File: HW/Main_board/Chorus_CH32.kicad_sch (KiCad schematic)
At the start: 88 parts, among them J1 DC_Jack, J2 Prog_Head, J3 Footswitch, J4 IN, J5 OUT, J6 Pot1, J7 Pot2, J8 UART, J9 9V, K1 G6KU-2, U1 AMS1117-5.0, U4 74LVC2G00, U6 TL072, U7 TL072, U8 TL072, U9 CH32V003AxMx

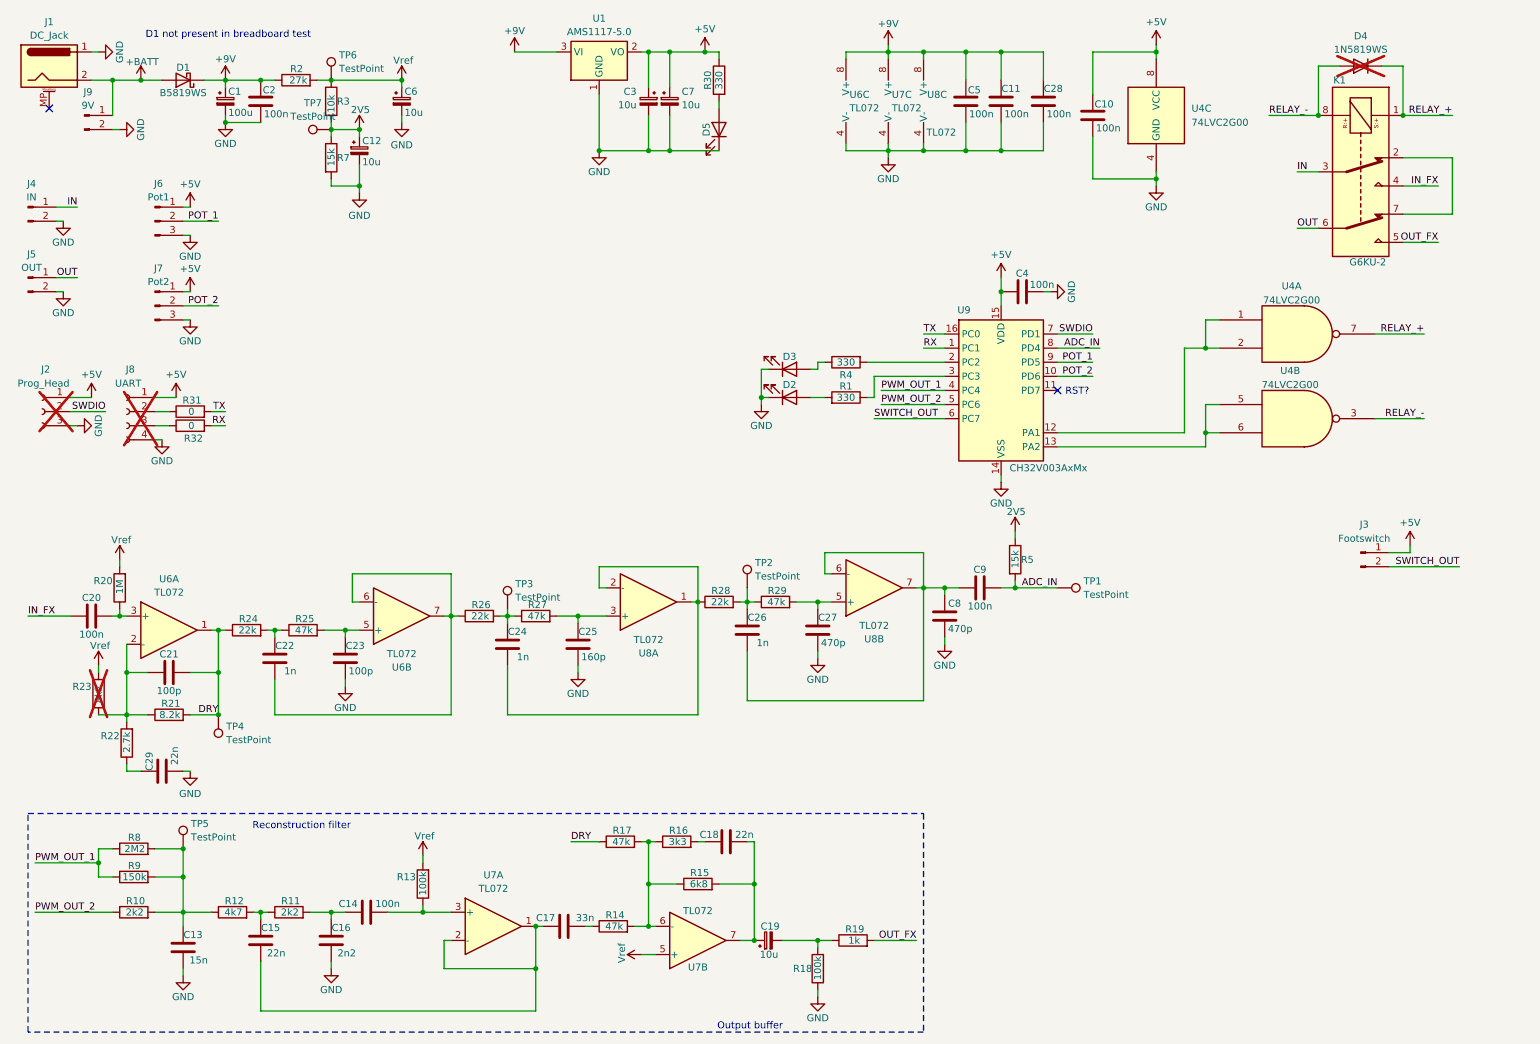
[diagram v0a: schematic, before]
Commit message: working passthrough code with dma + ouput buffer HW
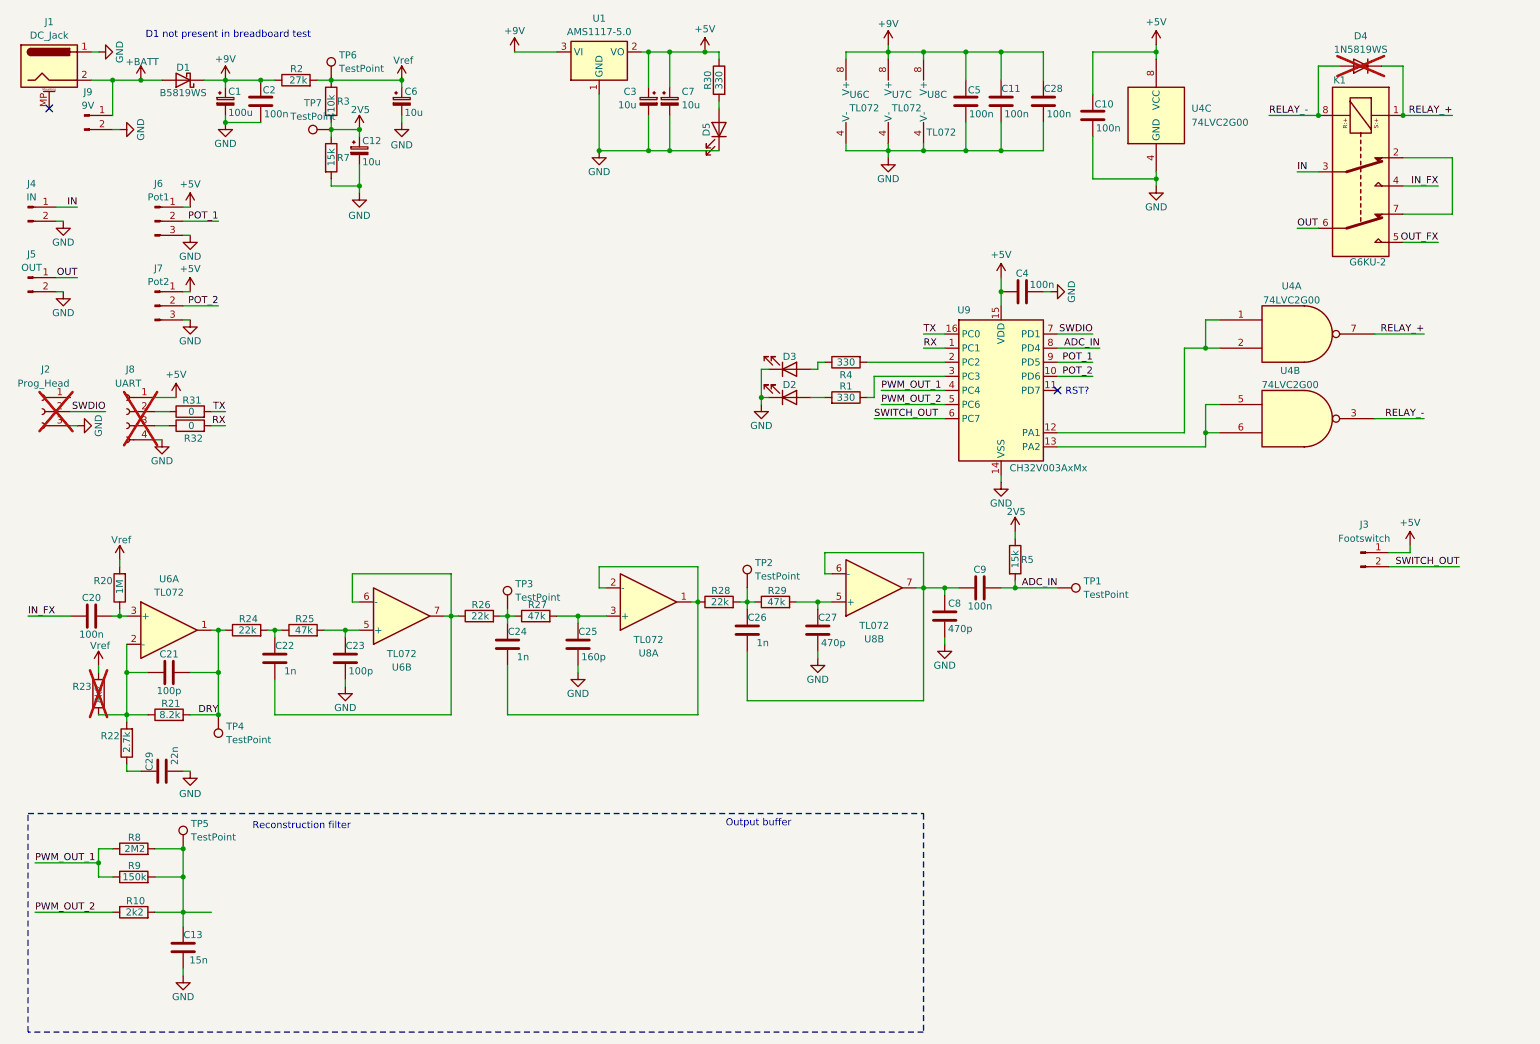
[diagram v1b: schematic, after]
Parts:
- removed C14: 100n, Capacitor_SMD:C_0603_1608Metric, symbol Device:C
- removed C15, C18: 22n, Capacitor_SMD:C_0603_1608Metric, symbol Device:C
- removed C16: 2n2, Capacitor_SMD:C_0603_1608Metric, symbol Device:C
- removed C17: 33n, Capacitor_SMD:C_0603_1608Metric, symbol Device:C
- removed C19: 10u, Capacitor_SMD:CP_Elec_5x5.4, symbol Device:C_Polarized_Small
- removed R11: 2k2, Resistor_SMD:R_0603_1608Metric, symbol Device:R
- removed R12: 4k7, Resistor_SMD:R_0603_1608Metric, symbol Device:R
- removed R13, R18: 100k, Resistor_SMD:R_0603_1608Metric, symbol Device:R
- removed R14, R17: 47k, Resistor_SMD:R_0603_1608Metric, symbol Device:R
- removed R15: 6k8, Resistor_SMD:R_0603_1608Metric, symbol Device:R
- removed R16: 3k3, Resistor_SMD:R_0603_1608Metric, symbol Device:R
- removed R19: 1k, Resistor_SMD:R_0603_1608Metric, symbol Device:R
- removed unit 1 of U7
- removed unit 2 of U7
- J3, J4, J5: footprint Connector_JST:JST_PH_B2B-PH-K_1x02_P2.00mm_Vertical -> Connector_PinHeader_2.54mm:PinHeader_1x02_P2.54mm_Vertical
- J6, J7: footprint Connector_JST:JST_PH_B3B-PH-K_1x03_P2.00mm_Vertical -> Connector_PinHeader_2.54mm:PinHeader_1x02_P2.54mm_Vertical
- J9: footprint Connector_JST:JST_PH_B2B-PH-K_1x02_P2.00mm_Vertical -> Connector_PinSocket_2.54mm:PinSocket_1x02_P2.54mm_Vertical
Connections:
- net +5V: no longer J2.1 (Pin_1)

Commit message: correction on output board and new main layout/schem
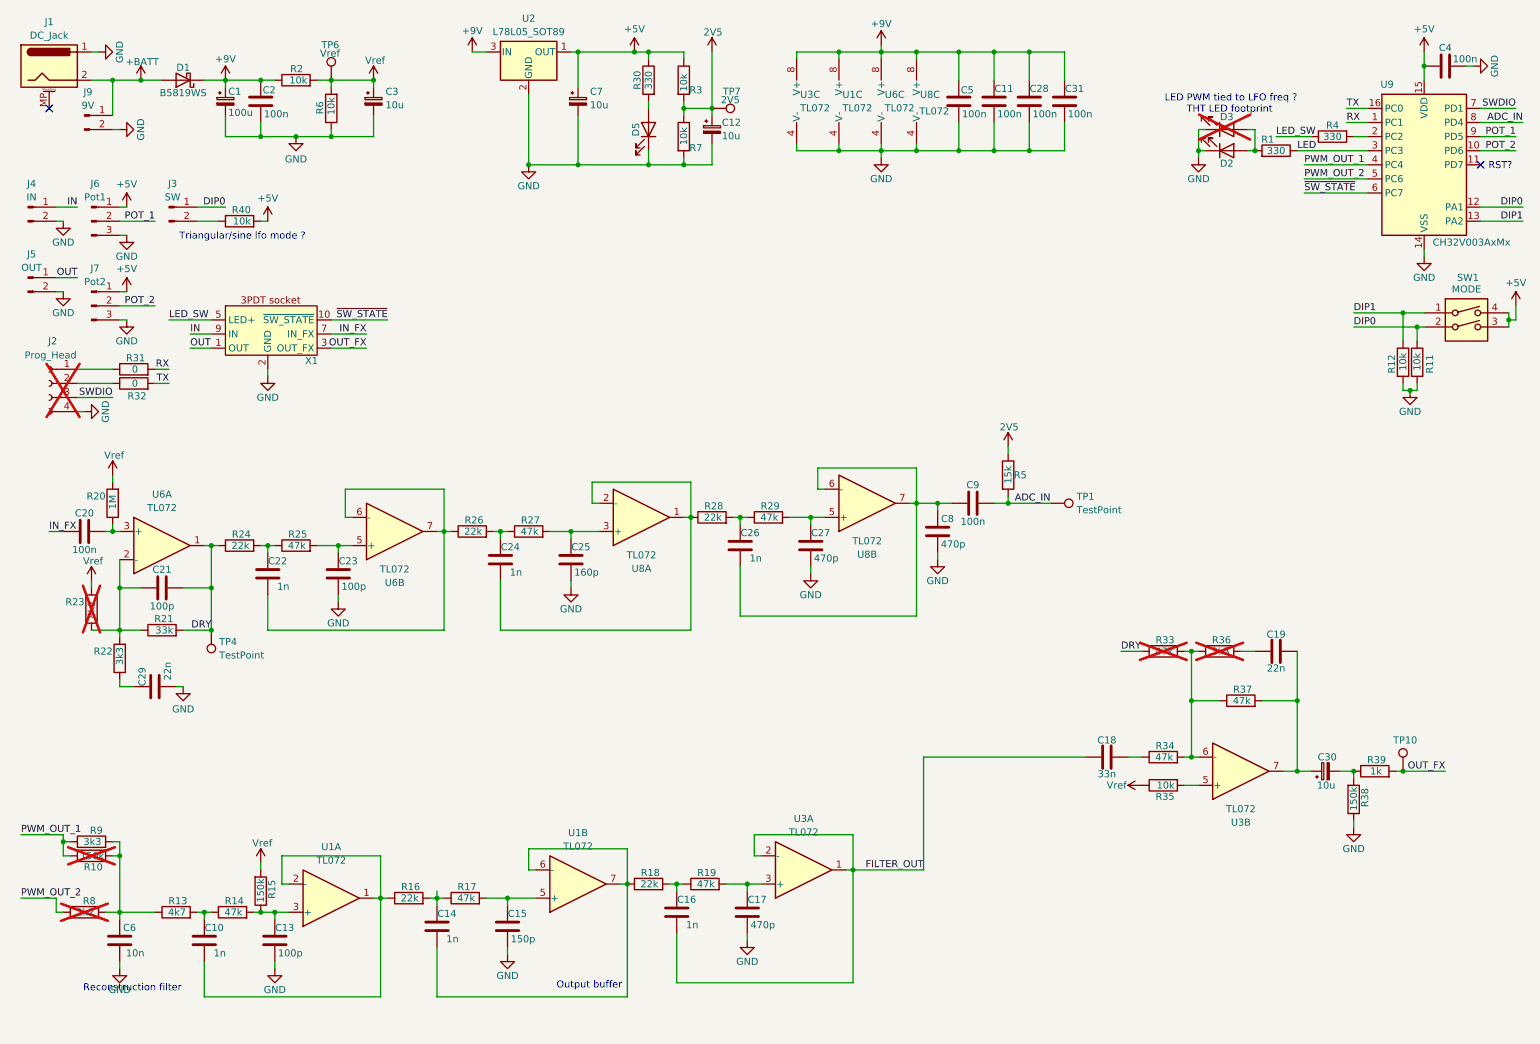
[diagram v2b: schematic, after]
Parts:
- removed C6: 10u, Capacitor_SMD:CP_Elec_5x5.4, symbol Device:C_Polarized_Small
- removed D4: 1N5819WS, Diode_SMD:D_SOD-323, symbol Device:D
- removed J8: UART, Connector_PinHeader_2.54mm:PinHeader_1x04_P2.54mm_Vertical, symbol Connector:Conn_01x04_Socket
- removed K1: G6KU-2, Relay_SMD:Relay_DPDT_Omron_G6K-2F-Y, symbol Relay:G6KU-2
- removed TP2, TP3, TP5: TestPoint, TestPoint:TestPoint_Pad_D1.0mm, symbol Connector:TestPoint
- removed U1: AMS1117-5.0, Package_TO_SOT_SMD:SOT-223-3_TabPin2, symbol Regulator_Linear:AMS1117-5.0
- removed U4: 74LVC2G00, Package_SO:VSSOP-8_2.3x2mm_P0.5mm, symbol 74xGxx:74LVC2G00
- removed U7: TL072, Package_SO:SOIC-8_3.9x4.9mm_P1.27mm, symbol Amplifier_Operational:TL072
- added C14, C16: 1n, Capacitor_SMD:C_0603_1608Metric, symbol Device:C
- added C15: 150p, Capacitor_SMD:C_0603_1608Metric, symbol Device:C
- added C17: 470p, Capacitor_SMD:C_0603_1608Metric, symbol Device:C
- added C18: 33n, Capacitor_SMD:C_0603_1608Metric, symbol Device:C
- added C19: 22n, Capacitor_SMD:C_0603_1608Metric, symbol Device:C
- added C30: 10u, Capacitor_SMD:CP_Elec_5x5.4, symbol Device:C_Polarized_Small
- added C31: 100n, Capacitor_SMD:C_0603_1608Metric, symbol Device:C
- added C6: 10n, Capacitor_SMD:C_0603_1608Metric, symbol Device:C
- added R11, R12, R35, R40, R6: 10k, Resistor_SMD:R_0603_1608Metric, symbol Device:R
- added R13: 4k7, Resistor_SMD:R_0603_1608Metric, symbol Device:R
- added R14, R17, R19, R33, R34, R37: 47k, Resistor_SMD:R_0603_1608Metric, symbol Device:R
- added R15, R38: 150k, Resistor_SMD:R_0603_1608Metric, symbol Device:R
- added R16, R18: 22k, Resistor_SMD:R_0603_1608Metric, symbol Device:R
- added R36: 3k3, Resistor_SMD:R_0603_1608Metric, symbol Device:R
- added R39: 1k, Resistor_SMD:R_0603_1608Metric, symbol Device:R
- added SW1: MODE, Button_Switch_SMD:SW_DIP_SPSTx02_Slide_KingTek_DSHP02TS_W7.62mm_P1.27mm, symbol Switch:SW_DIP_x02
- added TP10: TestPoint, TestPoint:TestPoint_Pad_D1.0mm, symbol Connector:TestPoint
- added U1, U3: TL072, Package_SO:SOIC-8_3.9x4.9mm_P1.27mm, symbol Amplifier_Operational:TL072
- added U2: L78L05_SOT89, Package_TO_SOT_SMD:SOT-89-3, symbol Regulator_Linear:L78L05_SOT89
- added X1: ~, Connector_PinHeader_1.27mm:PinHeader_1x10_P1.27mm_Vertical, symbol AREA_composant:3pdt_switch_connector
- C10: value 100n -> 1n
- C12: lcsc (none) -> C7171
- C13: value 15n -> 100p
- C3, C7: footprint Capacitor_Tantalum_SMD:CP_EIA-3216-18_Kemet-A -> Capacitor_SMD:CP_Elec_5x5.4
- D3: value LED -> CTL1; footprint LED_SMD:LED_0603_1608Metric -> Connector_PinSocket_1.27mm:PinSocket_1x02_P1.27mm_Vertical; now not fitted
- J2: footprint Connector_PinSocket_1.27mm:PinSocket_1x03_P1.27mm_Vertical -> Connector_PinHeader_1.27mm:PinHeader_1x04_P1.27mm_Vertical; symbol Connector:Conn_01x03_Socket -> Connector:Conn_01x04_Socket
- J3: value Footswitch -> SW; footprint Connector_PinHeader_2.54mm:PinHeader_1x02_P2.54mm_Vertical -> Connector_PinHeader_1.27mm:PinHeader_1x02_P1.27mm_Vertical
- J4, J5: footprint Connector_PinHeader_2.54mm:PinHeader_1x02_P2.54mm_Vertical -> Connector_PinHeader_1.27mm:PinHeader_1x02_P1.27mm_Vertical
- J6, J7: footprint Connector_PinHeader_2.54mm:PinHeader_1x02_P2.54mm_Vertical -> Connector_PinHeader_1.27mm:PinHeader_1x03_P1.27mm_Vertical
- J9: footprint Connector_PinSocket_2.54mm:PinSocket_1x02_P2.54mm_Vertical -> Connector_PinHeader_1.27mm:PinHeader_1x02_P1.27mm_Vertical
- R10: value 2k2 -> 150k; now not fitted
- R2: value 27k -> 10k
- R21: value 8.2k -> 33k
- R22: value 2.7k -> 3k3
- R7: value 15k -> 10k
- R8: value 2M2 -> 2k2; now not fitted
- R9: value 150k -> 3k3
- TP6: value TestPoint -> Vref
- TP7: value TestPoint -> 2V5
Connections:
- net +5V: now also R3.1, R40.2, SW1.3, SW1.4, U2.1 (OUT); no longer C10.1, C3.1, J3.1 (Pin_1)
- net +9V: now also C31.1, U1.8 (V+), U2.3 (IN), U3.8 (V+)
- net DRY: now also R33.1
- net GND: now also J2.4 (Pin_4), C15.2, C17.2, C31.2, C6.2, R11.2, R12.2, R38.1, R6.1, U1.4 (V-), U2.2 (GND), U3.4 (V-), X1.2 (GND), X1.4 (GND), X1.6 (GND), X1.8 (GND); no longer C10.2, J2.3 (Pin_3)
- net IN: now also X1.9 (IN)
- net IN_FX: now also X1.7 (IN_FX)
- net OUT: now also X1.1 (OUT)
- net OUT_FX: now also R39.2, TP10.1, X1.3 (OUT_FX)
- net PWM_OUT_1: now also R10.1; no longer R8.1
- net PWM_OUT_2: now also R8.1; no longer R10.1
- net RX: now also R31.2; no longer R32.2
- net SWDIO: now also J2.3 (Pin_3); no longer J2.2 (Pin_2)
- net TX: now also R32.2; no longer R31.2
- net Vref: now also C3.1, R15.2, R35.1, R6.2; no longer R3.1
- net at D2.2 (A), R1.2: now also D3.2 (A)
- net at R10.2, R8.2, R9.2: now also C6.1, R13.1; no longer C13.1
- net DIP1: now reaches U9.13 (PA2)
- net DIP1: now also R12.1, SW1.1
- net DIP0: now reaches U9.12 (PA1)
- net DIP0: now also J3.1 (Pin_1), R11.1, SW1.2
- net at J2.1 (Pin_1): now also R31.1
- net at R32.1: now also J2.2 (Pin_2)
- net LED: now reaches R1.1, U9.3 (PC3)
- net LED_SW: now reaches R4.1
- net LED_SW: now also X1.5 (LED+); no longer D3.2 (A)
- net SWITCH_OUT: no longer names the net of J3.2 (Pin_2)
- net SWITCH_OUT: now also R40.1; no longer U9.6 (PC7)
- new net: C16.1, R18.2, R19.1
- new net: C17.1, R19.2, U3.3 (+)
- new net: R35.2, U3.5 (+)
- new net: R33.2, R34.2, R36.1, R37.1, U3.6 (-)
- new net: C19.2, C30.1, R37.2, U3.7
- new net: C15.1, R17.2, U1.5 (+)
- new net: C14.2, R18.1, U1.6 (-), U1.7
- new net: C18.2, R34.1
- new net: C10.2, R16.1, U1.1, U1.2 (-)
- new net: C14.1, R16.2, R17.1
- new net: C10.1, R13.2, R14.1
- new net: C13.1, R14.2, R15.1, U1.3 (+)
- new net: C30.2, R38.2, R39.1
- new net: C19.1, R36.2
- new net FILTER_OUT: C16.2, C18.1, U3.1, U3.2 (-)
- new net ~{SW_STATE}: U9.6 (PC7), X1.10 (~{SW_STATE})
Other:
- note added: "LED PWM tied to LFO freq ?"
- note added: "THT LED footprint"
- note added: "Triangular/sine lfo mode ?"
- note removed: "D1 not present in breadboard test"
- moved on the sheet: C11, C20, C21, C22, C23, C24, C25, C26, C27, C28, C29, C4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

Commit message: improved PSU filtering
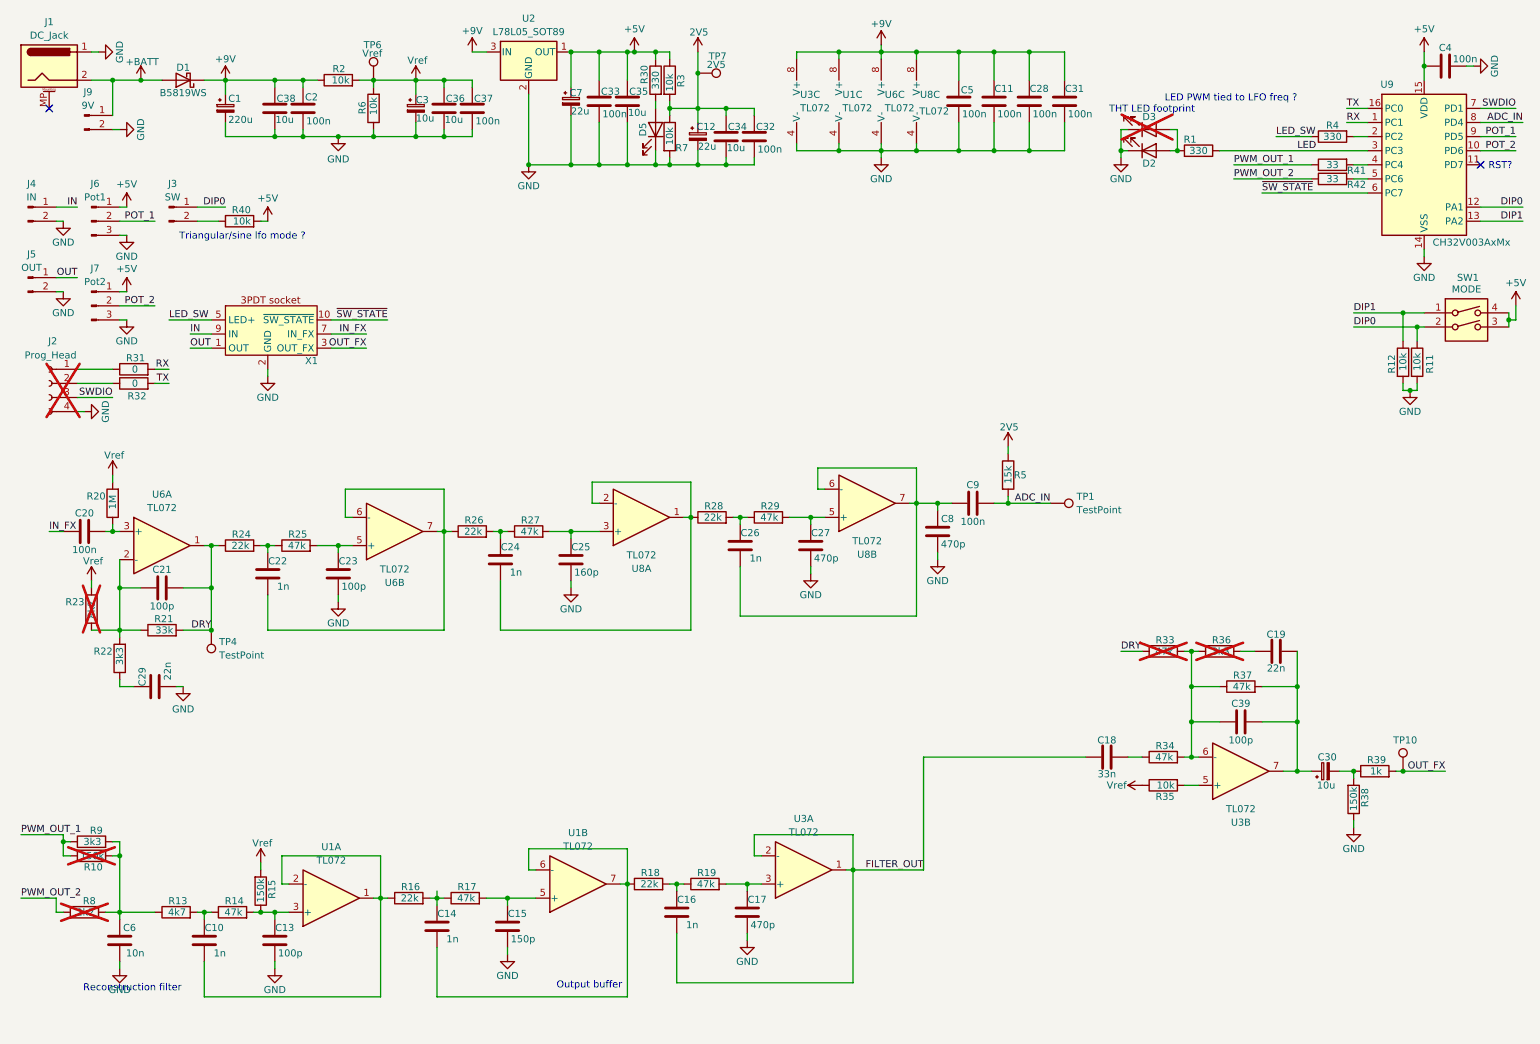
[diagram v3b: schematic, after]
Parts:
- added C32, C33, C37: 100n, Capacitor_SMD:C_0603_1608Metric, symbol Device:C
- added C34, C35, C36, C38: 10u, Capacitor_SMD:C_0603_1608Metric, symbol Device:C
- added C39: 100p, Capacitor_SMD:C_0603_1608Metric, symbol Device:C
- added R41, R42: 33, Resistor_SMD:R_0603_1608Metric, symbol Device:R
- C1: value 100u -> 220u
- C12, C7: value 10u -> 22u
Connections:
- net +5V: now also C33.1, C35.1
- net +9V: now also C38.1
- net 2V5: now also C32.1, C34.1
- net GND: now also C32.2, C33.2, C34.2, C35.2, C36.2, C37.2, C38.2
- net PWM_OUT_1: now also R41.1; no longer U9.4 (PC4)
- net PWM_OUT_2: now also R42.1; no longer U9.5 (PC6)
- net Vref: now also C36.1, C37.1
- net at R33.2, R34.2, R36.1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: now also C39.1
- net at C19.2, C30.1, R37.2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: now also C39.2
- new net: R42.2, U9.5 (PC6)
- new net: R41.2, U9.4 (PC4)
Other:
- moved on the sheet: C1, C12, C2, C3, C7, D2, D3, D5, R1, R2, R3, R30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
